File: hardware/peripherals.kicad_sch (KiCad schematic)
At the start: 0 parts

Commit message: Peripherals: add status LEDs, NeoPixel with 74AHCT1G125 level shifter
- Power LED (nLED_PWR) and activity LED (nLED_ACT) with resistors, DNP
- SK6812MINI-E NeoPixel with 74AHCT1G125 3.3V→5V level shifter
- 300Ω series resistor on NeoPixel data line
- 9 ERC errors remaining, all expected (undriven inputs on other sheets)
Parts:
- added D1: LED R, symbol Device:LED
- added D2: LED G, symbol Device:LED
- added D3: SK6812MINI-E, LED_SMD:LED_SK6812MINI-E_3.2x2.8mm_P1.5mm_ReverseMount, symbol LED:SK6812MINI-E
- added R1, R2: 2K2, symbol Device:R
- added R3: 220R, symbol Device:R
- added U1: 74AHCT1G125, symbol 74xGxx:74AHCT1G125
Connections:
- new net: D2.2 (A), R2.1
- new net: R3.1, U1.4
- new net: D1.2 (A), R1.1
- new net: D3.2 (DIN), R3.2
- new net +3V3: R1.2, R2.2
- new net +5VP: D3.3 (VDD), U1.5 (VCC)
- new net GND: D3.1 (VSS), U1.1, U1.3 (GND)
- new net NEOPIXEL: U1.2
- new net nLED_ACT: D2.1 (K)
- new net nLED_PWR: D1.1 (K)
- no-connect marks 0 -> 1

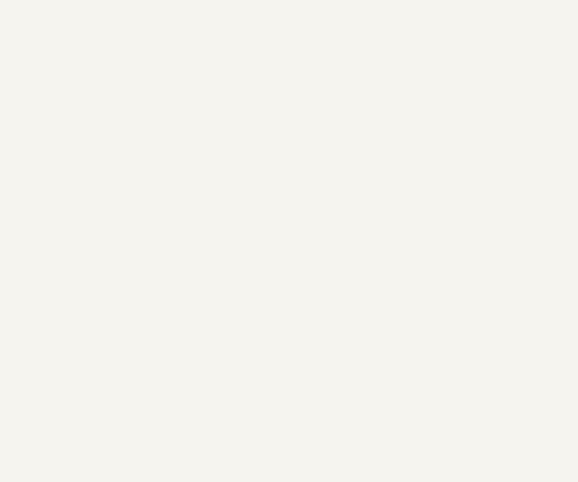
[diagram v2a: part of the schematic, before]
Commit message: Peripherals: add nRPIBOOT header and tactile button
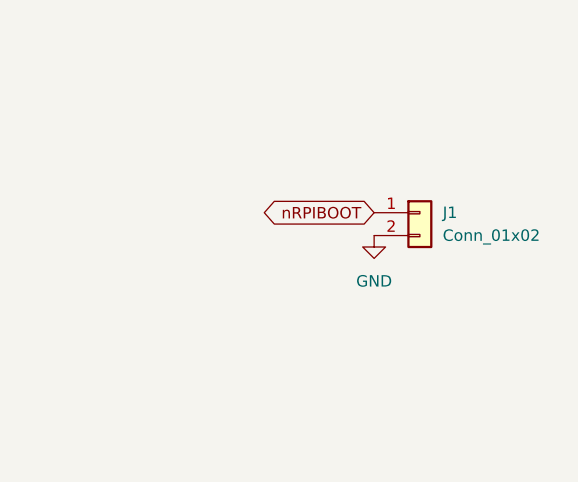
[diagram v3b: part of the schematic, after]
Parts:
- added J1: Conn_01x02, symbol Connector_Generic:Conn_01x02
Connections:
- net GND: now also J1.2 (Pin_2)
- new net nRPIBOOT: J1.1 (Pin_1)
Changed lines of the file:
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@@
+		)
+	)
+	(global_label "nRPIBOOT"
+		(shape bidirectional)
+		(at 195.58 38.1 180)
+		(fields_autoplaced yes)
+		(effects
+			(font
+				(size 1.27 1.27)
+			)
+			(justify right)
+		)
+		(property "Intersheetrefs" "${INTERSHEET_REFS}"
+			(at 182.2911 38.1 0)
+			(hide yes)
+			(show_name no)
+			(do_not_autoplace no)
+			(effects
+				(font
+					(size 1.27 1.27)
+				)
+				(justify right)
+			)
 		)
 	)
@@
 	)
 	(symbol
+		(lib_id "power:GND")
+		(at 195.58 40.64 0)
+		(unit 1)
+		(body_style 1)
+		(exclude_from_sim no)
+		(in_bom yes)
+		(on_board yes)
+		(in_pos_files yes)
+		(dnp no)
+		(fields_autoplaced yes)
+		(property "Reference" "#PWR012"
+			(at 195.58 46.99 0)
+			(hide yes)
+			(show_name no)
+			(do_not_autoplace no)
+			(effects
+				(font
+					(size 1.27 1.27)
+				)
+			)
+		)
+		(property "Value" "GND"
+			(at 195.58 45.72 0)
+			(show_name no)
+			(do_not_autoplace no)
+			(effects
+				(font
+					(size 1.27 1.27)
+				)
+			)
+		)
+		(property "Footprint" ""
+			(at 195.58 40.64 0)
+			(hide yes)
+			(show_name no)
+			(do_not_autoplace no)
+			(effects
+				(font
+					(size 1.27 1.27)
+				)
+			)
+		)
+		(property "Datasheet" ""
+			(at 195.58 40.64 0)
+			(hide yes)
+			(show_name no)
+			(do_not_autoplace no)
+			(effects
+				(font
+					(size 1.27 1.27)
+				)
+			)
+		)
+		(property "Description" "Power symbol creates a global label with name \"GND\" , ground"
+			(at 195.58 40.64 0)
+			(hide yes)
+			(show_name no)
+			(do_not_autoplace no)
+			(effects
+				(font
+					(size 1.27 1.27)
+				)
+			)
+		)
+		(pin "1"
+		)
+		(instances
+			(project "granit"
+				(path "/d2c135e3-a983-4cd4-8cff-b50ca3c7671a/d4e5f6a7-b8c9-4d0e-1f2a-3b4c5d6e7f80"
+					(reference "#PWR012")
+					(unit 1)
+				)
+			)
+		)
+	)
+	(symbol
 		(lib_id "Device:R")
 		(at 34.29 33.02 180)
@@
 					(unit 1)
 				)
+			)
+		)
+	)
+	(symbol
+		(lib_id "Connector_Generic:Conn_01x02")
+		(at 200.66 38.1 0)
+		(unit 1)
+		(body_style 1)
+		(exclude_from_sim no)
+		(in_bom yes)
+		(on_board yes)
+		(in_pos_files yes)
+		(dnp no)
+		(fields_autoplaced yes)
+		(property "Reference" "J1"
+			(at 203.2 38.0999 0)
+			(show_name no)
+			(do_not_autoplace no)
+			(effects
+				(font
+					(size 1.27 1.27)
+				)
+				(justify left)
+			)
+		)
+		(property "Value" "Conn_01x02"
+			(at 203.2 40.6399 0)
+			(show_name no)
+			(do_not_autoplace no)
+			(effects
+				(font
+					(size 1.27 1.27)
+				)
+				(justify left)
+			)
+		)
+		(property "Footprint" ""
+			(at 200.66 38.1 0)
+			(hide yes)
+			(show_name no)
+			(do_not_autoplace no)
+			(effects
+				(font
+					(size 1.27 1.27)
+				)
+			)
+		)
+		(property "Datasheet" ""
+			(at 200.66 38.1 0)
+			(hide yes)
+			(show_name no)
+			(do_not_autoplace no)
+			(effects
+				(font
+					(size 1.27 1.27)
+				)
+			)
+		)
+		(property "Description" "Generic connector, single row, 01x02, script generated (kicad-library-utils/schlib/autogen/connector/)"
+			(at 200.66 38.1 0)
+			(hide yes)
+			(show_name no)
+			(do_not_autoplace no)
+			(effects
+				(font
+					(size 1.27 1.27)
+				)
+			)
+		)
+		(pin "2"
+		)
+		(pin "1"
+		)
+		(instances
+			(project "granit"
+				(path "/d2c135e3-a983-4cd4-8cff-b50ca3c7671a/d4e5f6a7-b8c9-4d0e-1f2a-3b4c5d6e7f80"
+					(reference "J1")
+					(unit 1)
+				)

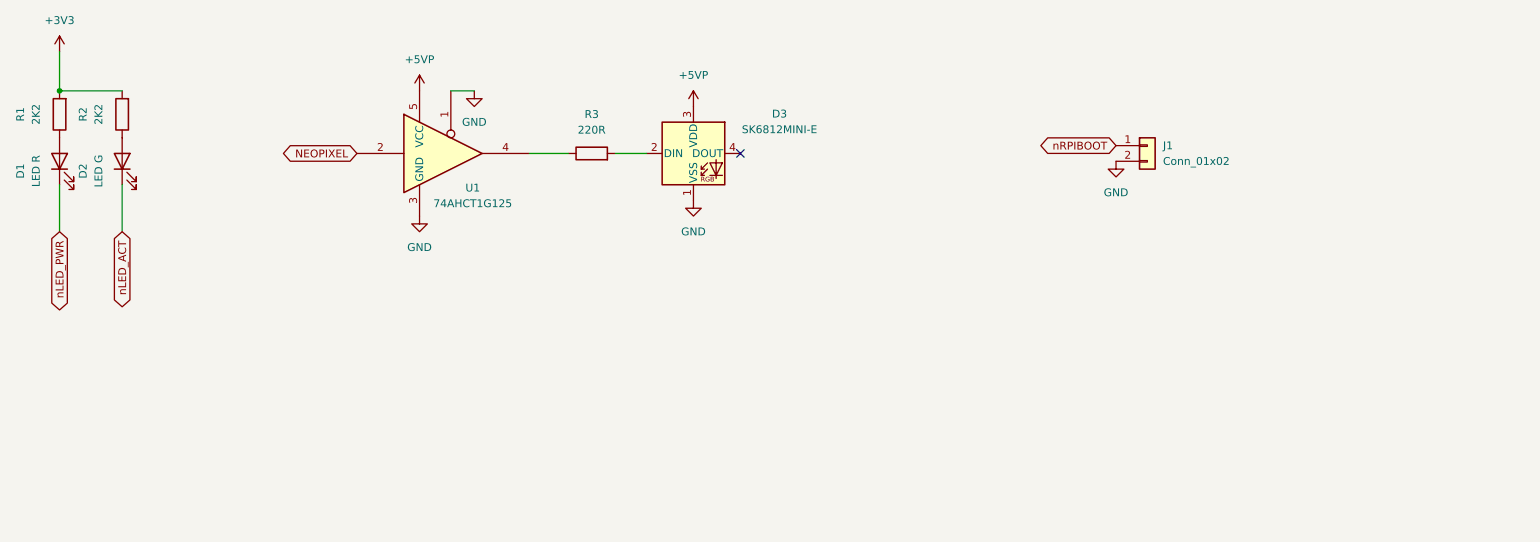
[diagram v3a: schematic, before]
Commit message: Peripherals: add UART debug header
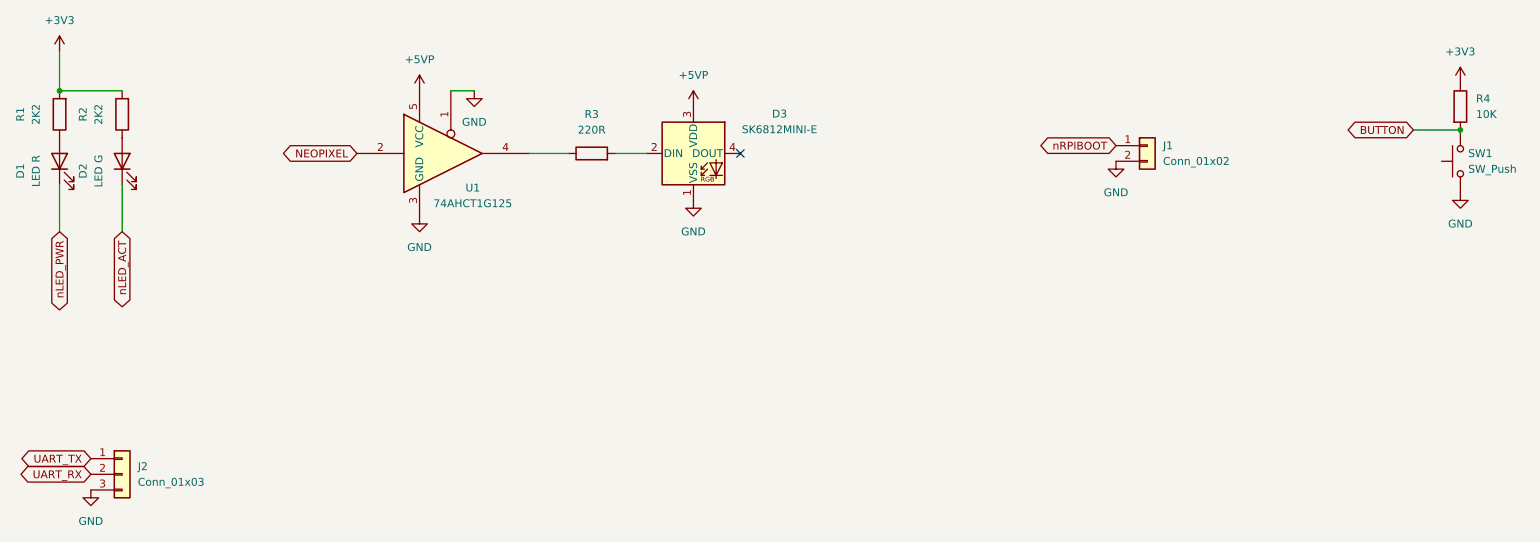
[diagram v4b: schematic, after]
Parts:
- added J2: Conn_01x03, symbol Connector_Generic:Conn_01x03
- added R4: 10K, symbol Device:R
- added SW1: SW_Push, symbol Switch:SW_Push
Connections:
- net +3V3: now also R4.1
- net GND: now also J2.3 (Pin_3), SW1.1
- new net BUTTON: R4.2, SW1.2
- new net UART_RX: J2.2 (Pin_2)
- new net UART_TX: J2.1 (Pin_1)

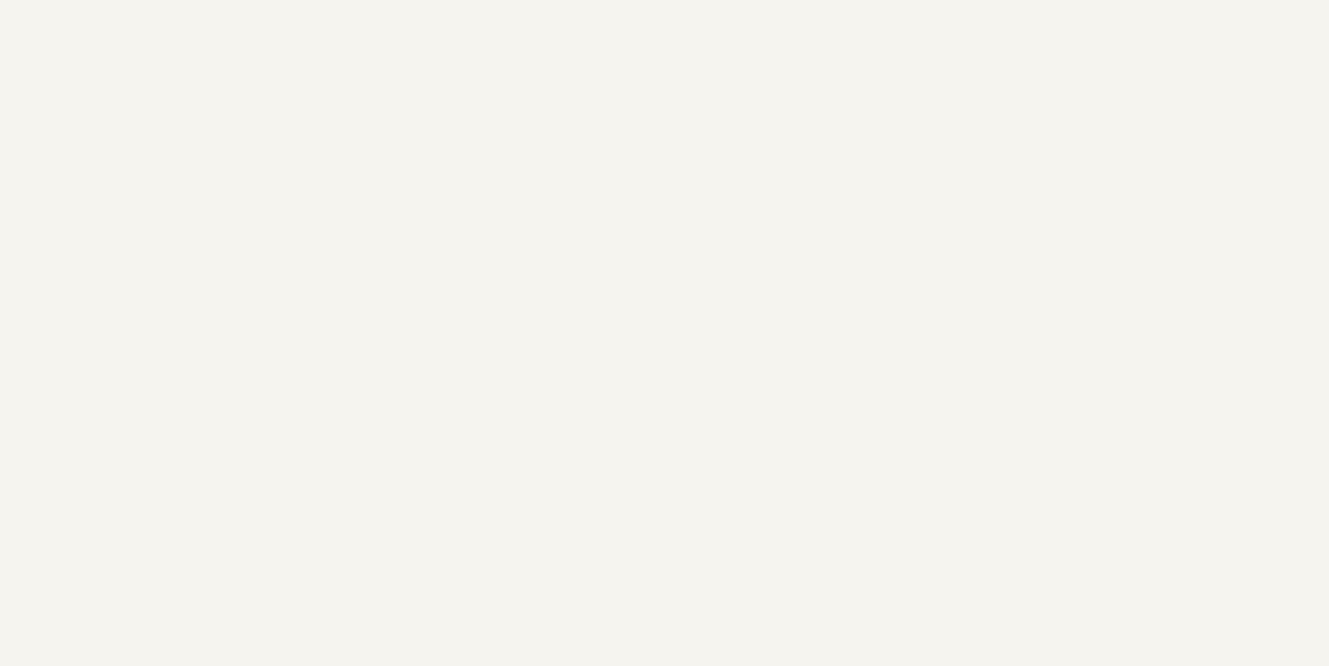
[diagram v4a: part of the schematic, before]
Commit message: Peripherals: add DS3231MZ RTC with CR2032 battery backup
- DS3231MZ (SO-8) with I2C pull-ups (4.7kΩ)
- CR2032 battery holder for VBAT + PWR_FLAG
- INT/SQW connected to RTC_INT with pull-up
- 100nF decoupling cap on VCC
- Peripherals sheet complete: LEDs, NeoPixel, button, UART,
  nRPIBOOT header, RTC
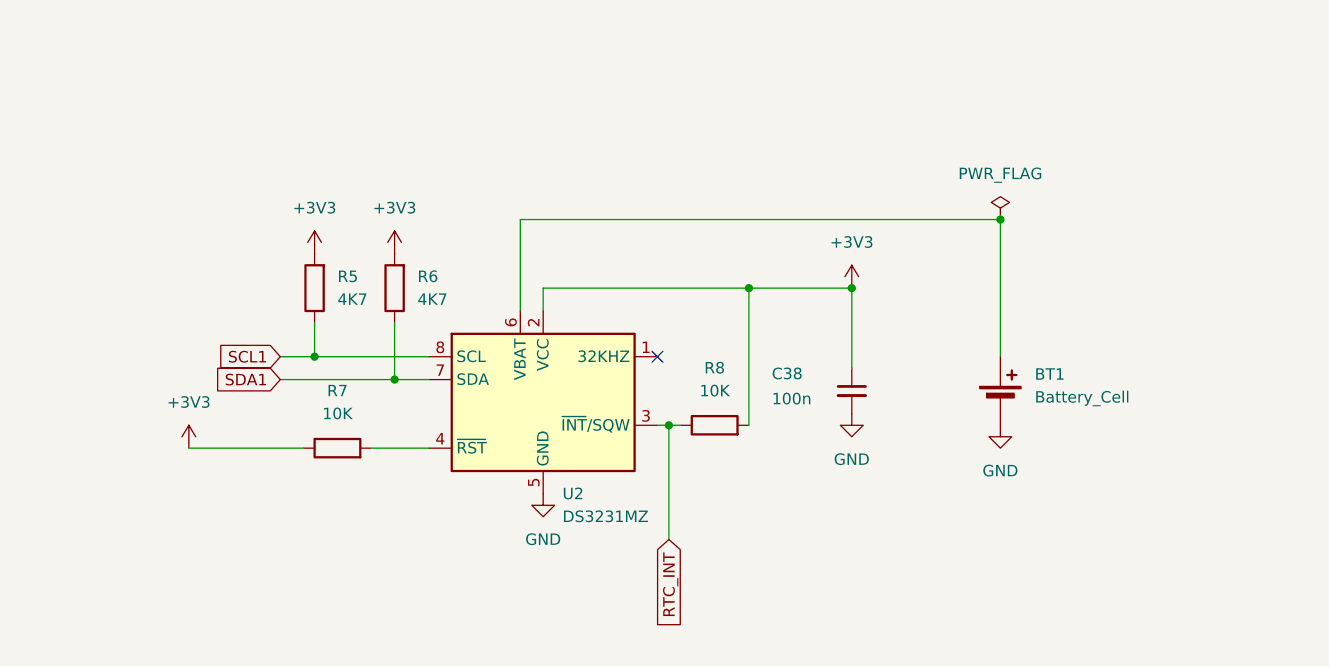
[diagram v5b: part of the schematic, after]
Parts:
- added BT1: Battery_Cell, symbol Device:Battery_Cell
- added C38: 100n, Capacitor_SMD:C_0805_2012Metric, symbol Device:C_Small
- added R5, R6: 4K7, symbol Device:R
- added R7, R8: 10K, symbol Device:R
- added U2: DS3231MZ, Package_SO:SOIC-8_3.9x4.9mm_P1.27mm, symbol Timer_RTC:DS3231MZ
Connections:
- net +3V3: now also C38.1, R5.2, R6.2, R7.1, R8.2, U2.2 (VCC)
- net GND: now also BT1.2 (-), C38.2, U2.5 (GND)
- new net: R7.2, U2.4 (~{RST})
- new net: BT1.1 (+), U2.6 (VBAT)
- new net RTC_INT: R8.1, U2.3 (~{INT}/SQW)
- new net SCL1: R5.1, U2.8 (SCL)
- new net SDA1: R6.1, U2.7 (SDA)
- no-connect marks 1 -> 2

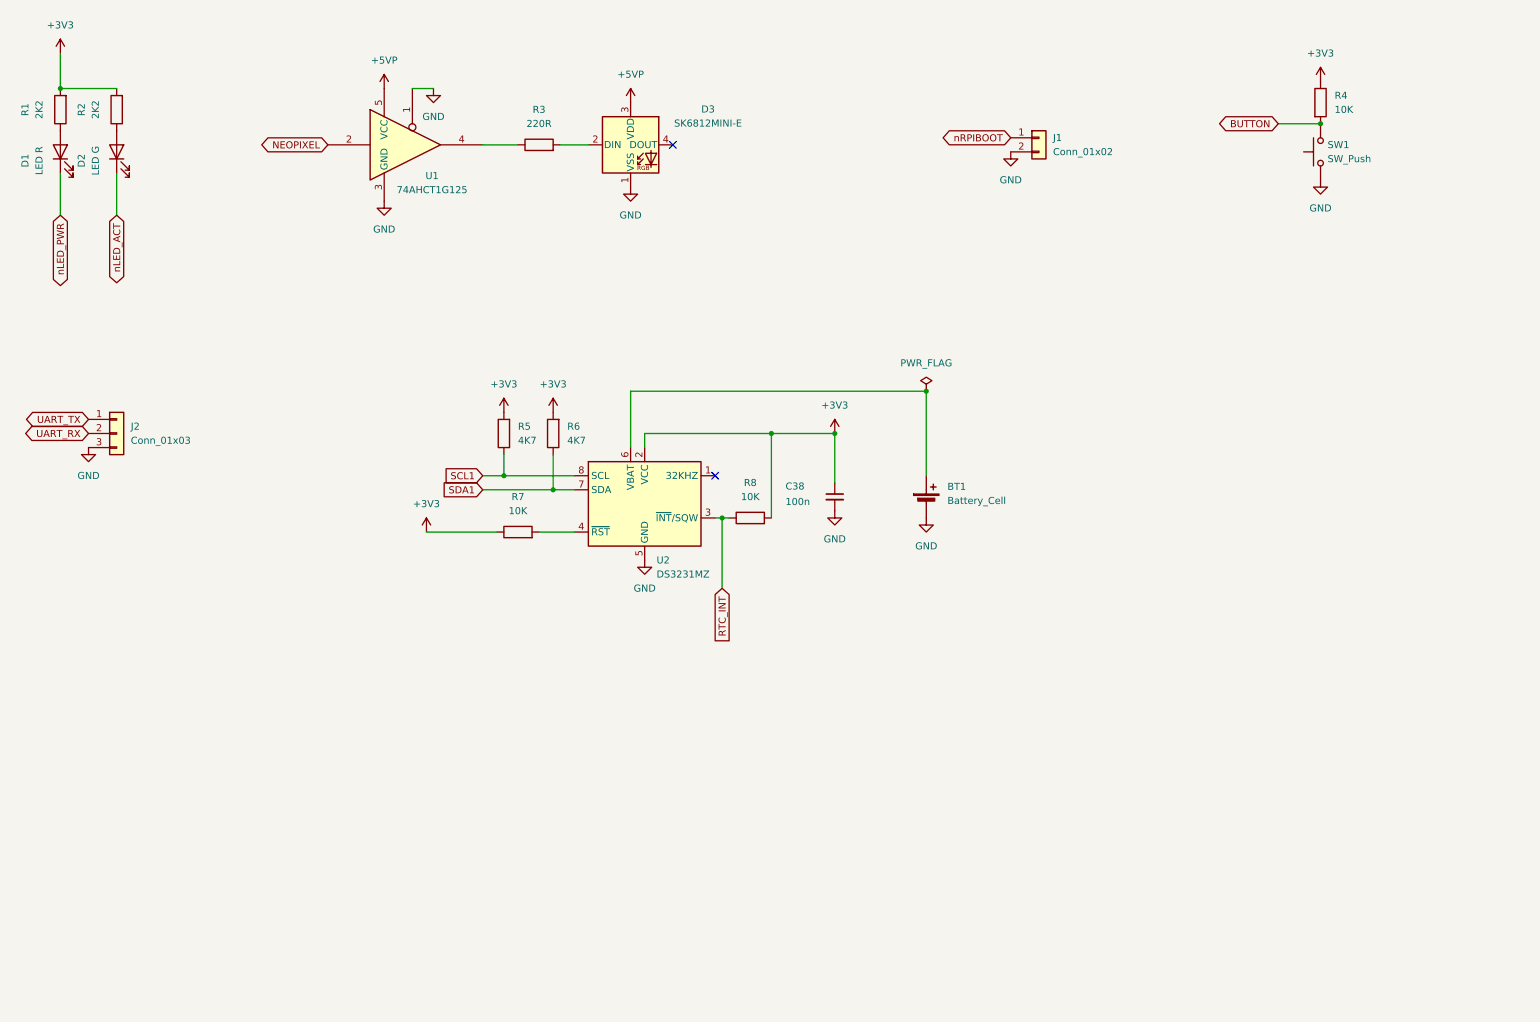
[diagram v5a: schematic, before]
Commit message: Peripherals: add USB-C OTG with USBLC6-2SC6 ESD protection
- USB-C receptacle (USB 2.0 only)
- USBLC6-2SC6 ESD protection on D+/D-
- 5.1kΩ CC pull-downs for device/sink identification
- USB_OTG_ID tied low for device mode
- 100nF shield-to-GND coupling cap
- Peripherals sheet complete
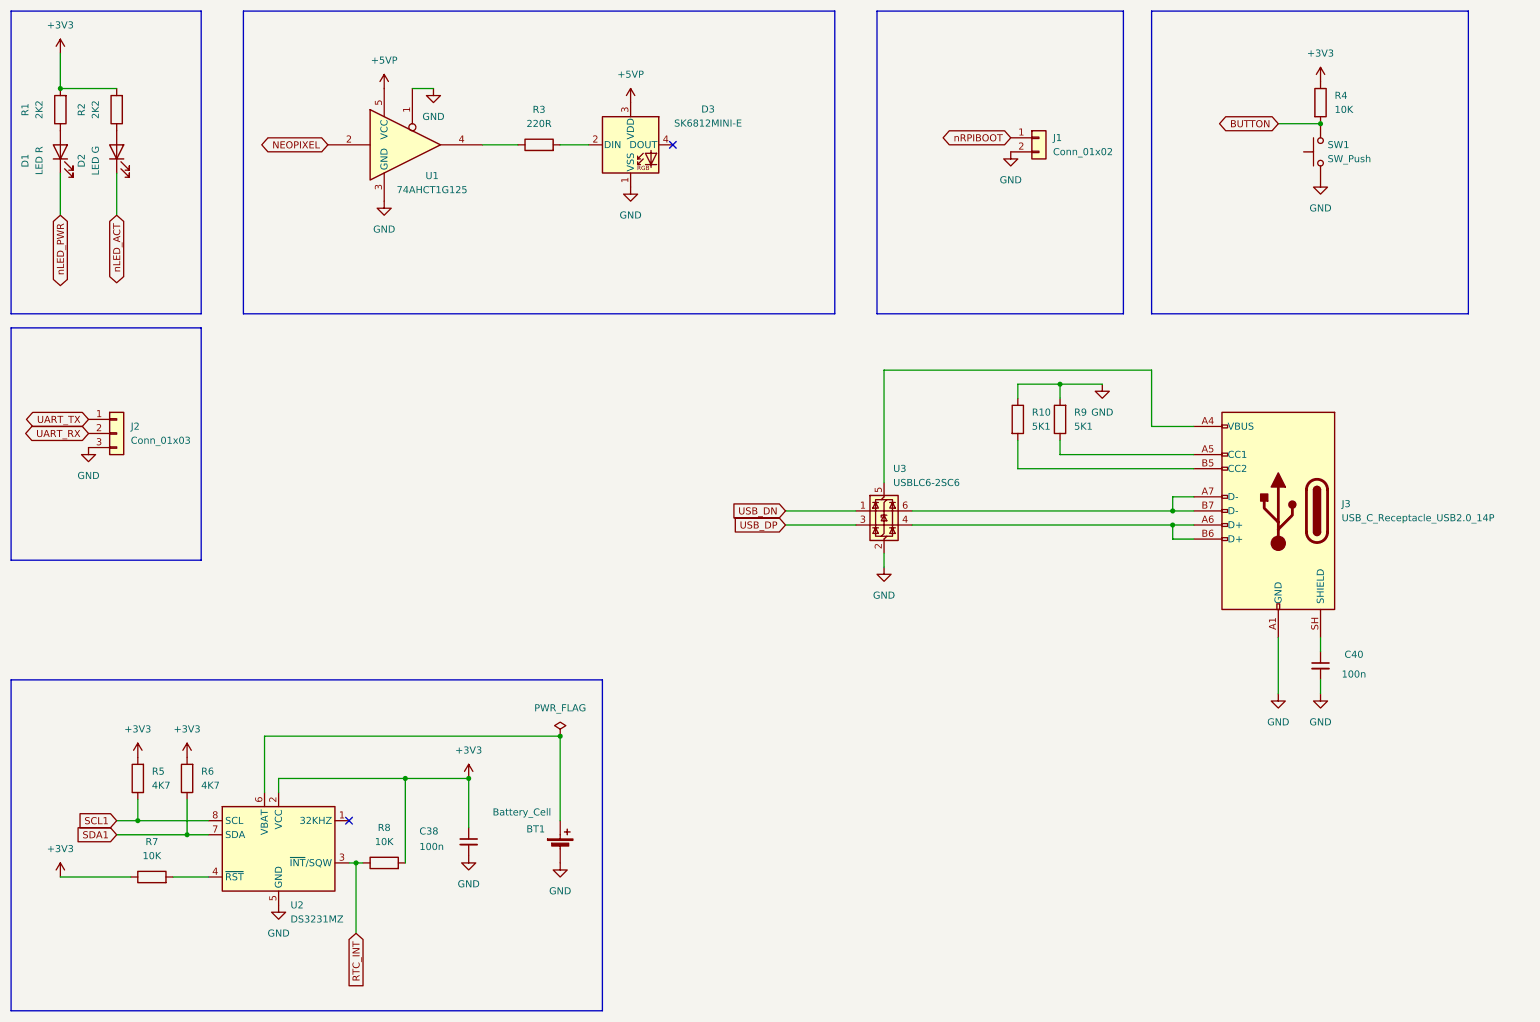
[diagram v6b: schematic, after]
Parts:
- added C40: 100n, Capacitor_SMD:C_0805_2012Metric, symbol Device:C_Small
- added J3: USB_C_Receptacle_USB2.0_14P, symbol Connector:USB_C_Receptacle_USB2.0_14P
- added R10, R9: 5K1, symbol Device:R
- added U3: USBLC6-2SC6, Package_TO_SOT_SMD:SOT-23-6, symbol Power_Protection:USBLC6-2SC6
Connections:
- net GND: now also C40.2, J3.A1 (GND), J3.A12 (GND), J3.B1 (GND), J3.B12 (GND), R10.1, R9.2, U3.2 (GND)
- new net: J3.A6 (D+), J3.B6 (D+), U3.4 (I/O2)
- new net: J3.A4 (VBUS), J3.A9 (VBUS), J3.B4 (VBUS), J3.B9 (VBUS), U3.5 (VBUS)
- new net: J3.A7 (D-), J3.B7 (D-), U3.6 (I/O1)
- new net: J3.A5 (CC1), R9.1
- new net: C40.1, J3.SH (SHIELD)
- new net: J3.B5 (CC2), R10.2
- new net USB_DN: U3.1 (I/O1)
- new net USB_DP: U3.3 (I/O2)
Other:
- moved on the sheet: BT1, C38, R5, R6, R7, R8, U2
